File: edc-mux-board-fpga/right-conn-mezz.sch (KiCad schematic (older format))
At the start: 86 parts, among them J21 Device 10, J22 Device 13, J23 Device 11, J24 Device 14, J25 Left Mezzanine Board Connecto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, J26 Left Mezzanine Board Connecto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, J27 Device 12, J28 Device 15

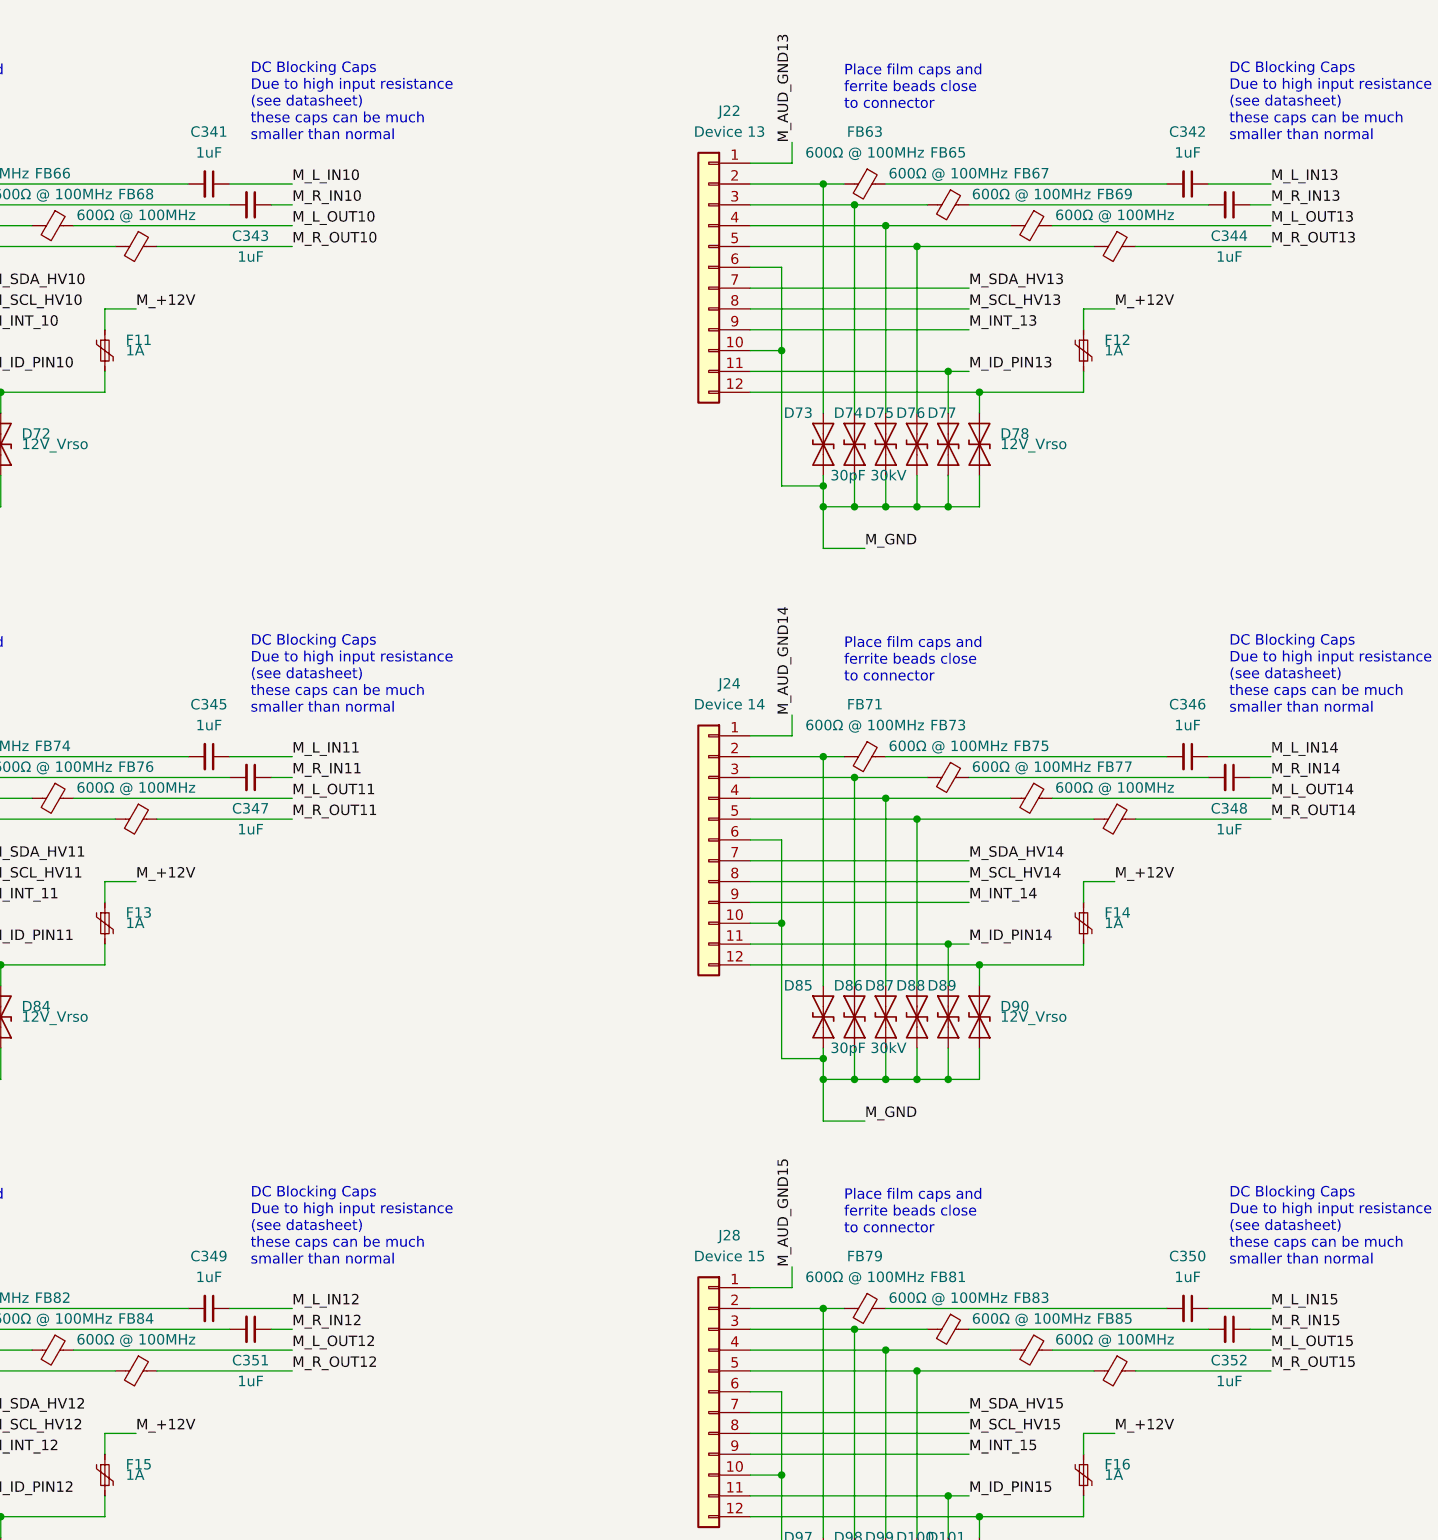
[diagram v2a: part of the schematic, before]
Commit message: assigned more footprints
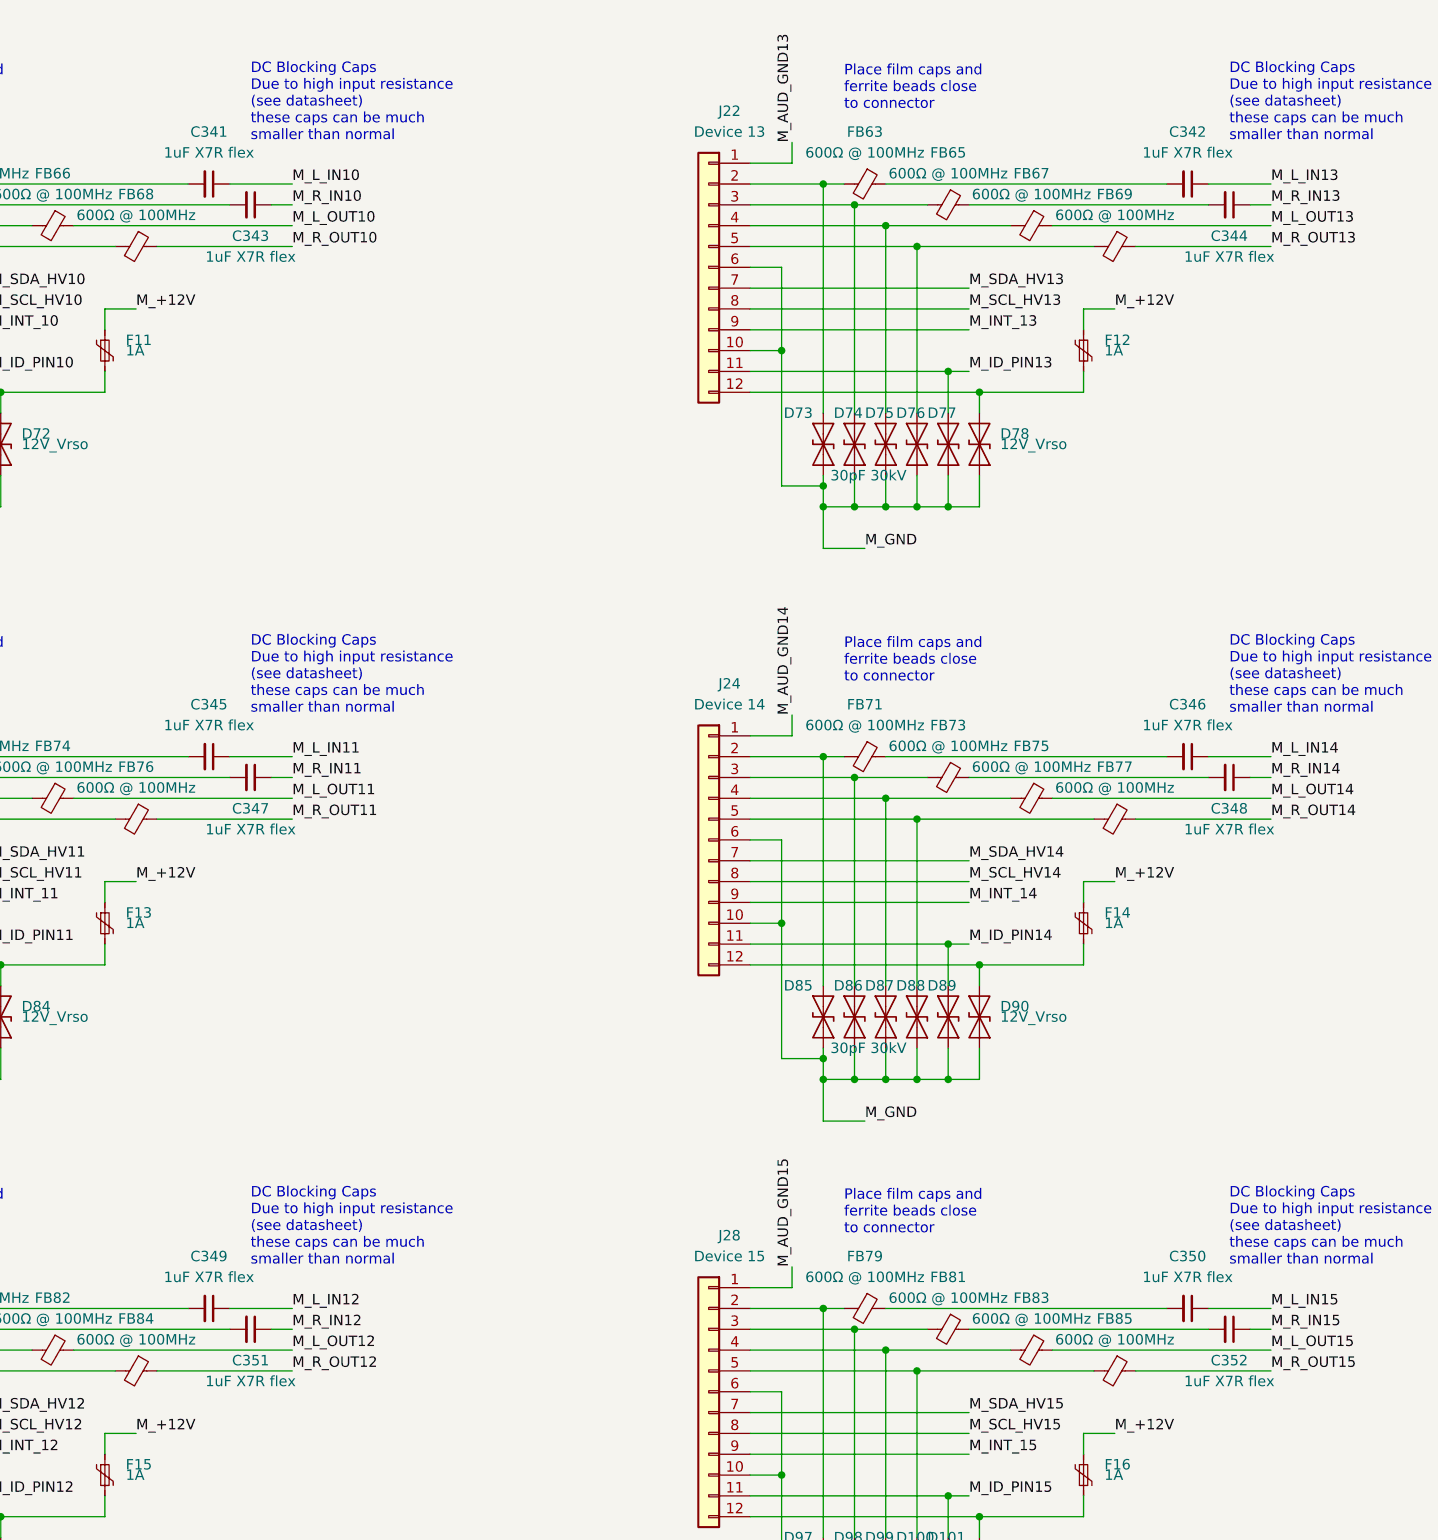
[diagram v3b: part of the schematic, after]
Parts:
- C341, C342, C343, C344, C345, C346, C347, C348, C349, C350, C351, C352: value 1uF -> 1uF X7R flex
- J21, J22, J23, J24, J27, J28: footprint Connector_PinHeader_1.27mm:PinHeader_2x06_P1.27mm_Vertical -> SW-TEConn:T4141012121-000; Manufacturer (none) -> TE Connectivity; Manufacturers Part Number (none) -> T4141012121-000
- J25: footprint (none) -> Connector_PinSocket_2.54mm:PinSocket_2x10_P2.54mm_Horizontal
- J26: footprint (none) -> Connector_PinHeader_2.54mm:PinHeader_2x10_P2.54mm_Vertical
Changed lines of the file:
@@
 F 0 "J21" H 700 2750 50  0000 C CNN
 F 1 "Device 10" H 700 2650 50  0000 C CNN
-F 2 "Connector_PinHeader_1.27mm:PinHeader_2x06_P1.27mm_Vertical" H 800 2000 50  0001 C CNN
-F 3 "~" H 800 2000 50  0001 C CNN
+F 2 "SW-TEConn:T4141012121-000" H 800 2000 50  0001 C CNN
+F 3 "https://www.te.com/commerce/DocumentDelivery/DDEController?Action=showdoc&DocId=Customer+Drawing%7FT4141012081000%7FA1%7Fpdf%7FEnglish%7FENG_CD_T4141012081000_A1.pdf%7FT4141012121-000" H 800 2000 50  0001 C CNN
+F 4 "TE Connectivity" H 0   0   50  0001 C CNN "Manufacturer"
+F 5 "T4141012121-000" H 0   0   50  0001 C CNN "Manufacturers Part Number"
 	1    800  2000
 	-1   0    0    -1
@@
 AR Path="/5CBF628A/61B47D43" Ref="C343"  Part="1"
 F 0 "C343" V 3450 1700 50  0000 C CNN
-F 1 "1uF" V 3550 1700 50  0000 C CNN
+F 1 "1uF X7R flex" V 3550 1700 50  0000 C CNN
 F 2 "Capacitor_SMD:C_0805_2012Metric" H 3300 1700 50  0001 C CNN
 F 3 "~" H 3300 1700 50  0001 C CNN
@@
 AR Path="/5CBF628A/61B47D54" Ref="C341"  Part="1"
 F 0 "C341" V 2850 1600 50  0000 C CNN
-F 1 "1uF" V 2950 1600 50  0000 C CNN
+F 1 "1uF X7R flex" V 2950 1600 50  0000 C CNN
 F 2 "Capacitor_SMD:C_0805_2012Metric" H 3100 1600 50  0001 C CNN
 F 3 "~" H 3100 1600 50  0001 C CNN
@@
 F 0 "J25" H 10450 7150 50  0000 C CNN
 F 1 "Left Mezzanine Board Connector (Daughterboard)" H 10450 3050 50  0000 C CNN
-F 2 "" H 10400 5150 50  0001 C CNN
+F 2 "Connector_PinSocket_2.54mm:PinSocket_2x10_P2.54mm_Horizontal" H 10400 5150 50  0001 C CNN
 F 3 "~" H 10400 5150 50  0001 C CNN
 	1    10400 5150
@@
 F 0 "J23" H 700 5500 50  0000 C CNN
 F 1 "Device 11" H 700 5400 50  0000 C CNN
-F 2 "Connector_PinHeader_1.27mm:PinHeader_2x06_P1.27mm_Vertical" H 800 4750 50  0001 C CNN
-F 3 "~" H 800 4750 50  0001 C CNN
+F 2 "SW-TEConn:T4141012121-000" H 800 4750 50  0001 C CNN
+F 3 "https://www.te.com/commerce/DocumentDelivery/DDEController?Action=showdoc&DocId=Customer+Drawing%7FT4141012081000%7FA1%7Fpdf%7FEnglish%7FENG_CD_T4141012081000_A1.pdf%7FT4141012121-000" H 800 4750 50  0001 C CNN
+F 4 "TE Connectivity" H 0   0   50  0001 C CNN "Manufacturer"
+F 5 "T4141012121-000" H 0   0   50  0001 C CNN "Manufacturers Part Number"
 	1    800  4750
 	-1   0    0    -1
@@
 AR Path="/5CBF628A/61B47E23" Ref="C347"  Part="1"
 F 0 "C347" V 3450 4450 50  0000 C CNN
-F 1 "1uF" V 3550 4450 50  0000 C CNN
+F 1 "1uF X7R flex" V 3550 4450 50  0000 C CNN
 F 2 "Capacitor_SMD:C_0805_2012Metric" H 3300 4450 50  0001 C CNN
 F 3 "~" H 3300 4450 50  0001 C CNN
@@
 AR Path="/5CBF628A/61B47E34" Ref="C345"  Part="1"
 F 0 "C345" V 2850 4350 50  0000 C CNN
-F 1 "1uF" V 2950 4350 50  0000 C CNN
+F 1 "1uF X7R flex" V 2950 4350 50  0000 C CNN
 F 2 "Capacitor_SMD:C_0805_2012Metric" H 3100 4350 50  0001 C CNN
 F 3 "~" H 3100 4350 50  0001 C CNN
@@
 F 0 "J27" H 700 8150 50  0000 C CNN
 F 1 "Device 12" H 700 8050 50  0000 C CNN
-F 2 "Connector_PinHeader_1.27mm:PinHeader_2x06_P1.27mm_Vertical" H 800 7400 50  0001 C CNN
-F 3 "~" H 800 7400 50  0001 C CNN
+F 2 "SW-TEConn:T4141012121-000" H 800 7400 50  0001 C CNN
+F 3 "https://www.te.com/commerce/DocumentDelivery/DDEController?Action=showdoc&DocId=Customer+Drawing%7FT4141012081000%7FA1%7Fpdf%7FEnglish%7FENG_CD_T4141012081000_A1.pdf%7FT4141012121-000" H 800 7400 50  0001 C CNN
+F 4 "TE Connectivity" H 0   0   50  0001 C CNN "Manufacturer"
+F 5 "T4141012121-000" H 0   0   50  0001 C CNN "Manufacturers Part Number"
 	1    800  7400
 	-1   0    0    -1
@@
 AR Path="/5CBF628A/61B47EF4" Ref="C351"  Part="1"
 F 0 "C351" V 3450 7100 50  0000 C CNN
-F 1 "1uF" V 3550 7100 50  0000 C CNN
+F 1 "1uF X7R flex" V 3550 7100 50  0000 C CNN
 F 2 "Capacitor_SMD:C_0805_2012Metric" H 3300 7100 50  0001 C CNN
 F 3 "~" H 3300 7100 50  0001 C CNN
@@
 AR Path="/5CBF628A/61B47F05" Ref="C349"  Part="1"
 F 0 "C349" V 2850 7000 50  0000 C CNN
-F 1 "1uF" V 2950 7000 50  0000 C CNN
+F 1 "1uF X7R flex" V 2950 7000 50  0000 C CNN
 F 2 "Capacitor_SMD:C_0805_2012Metric" H 3100 7000 50  0001 C CNN
 F 3 "~" H 3100 7000 50  0001 C CNN
@@
 F 0 "J22" H 5400 2750 50  0000 C CNN
 F 1 "Device 13" H 5400 2650 50  0000 C CNN
-F 2 "Connector_PinHeader_1.27mm:PinHeader_2x06_P1.27mm_Vertical" H 5500 2000 50  0001 C CNN
-F 3 "~" H 5500 2000 50  0001 C CNN
+F 2 "SW-TEConn:T4141012121-000" H 5500 2000 50  0001 C CNN
+F 3 "https://www.te.com/commerce/DocumentDelivery/DDEController?Action=showdoc&DocId=Customer+Drawing%7FT4141012081000%7FA1%7Fpdf%7FEnglish%7FENG_CD_T4141012081000_A1.pdf%7FT4141012121-000" H 5500 2000 50  0001 C CNN
+F 4 "TE Connectivity" H 0   0   50  0001 C CNN "Manufacturer"
+F 5 "T4141012121-000" H 0   0   50  0001 C CNN "Manufacturers Part Number"
 	1    5500 2000
 	-1   0    0    -1
@@
 AR Path="/5CBF628A/61B47FC5" Ref="C344"  Part="1"
 F 0 "C344" V 8150 1700 50  0000 C CNN
-F 1 "1uF" V 8250 1700 50  0000 C CNN
+F 1 "1uF X7R flex" V 8250 1700 50  0000 C CNN
 F 2 "Capacitor_SMD:C_0805_2012Metric" H 8000 1700 50  0001 C CNN
 F 3 "~" H 8000 1700 50  0001 C CNN
@@
 AR Path="/5CBF628A/61B47FD6" Ref="C342"  Part="1"
 F 0 "C342" V 7550 1600 50  0000 C CNN
-F 1 "1uF" V 7650 1600 50  0000 C CNN
+F 1 "1uF X7R flex" V 7650 1600 50  0000 C CNN
 F 2 "Capacitor_SMD:C_0805_2012Metric" H 7800 1600 50  0001 C CNN
 F 3 "~" H 7800 1600 50  0001 C CNN
@@
 F 0 "J24" H 5400 5500 50  0000 C CNN
 F 1 "Device 14" H 5400 5400 50  0000 C CNN
-F 2 "Connector_PinHeader_1.27mm:PinHeader_2x06_P1.27mm_Vertical" H 5500 4750 50  0001 C CNN
-F 3 "~" H 5500 4750 50  0001 C CNN
+F 2 "SW-TEConn:T4141012121-000" H 5500 4750 50  0001 C CNN
+F 3 "https://www.te.com/commerce/DocumentDelivery/DDEController?Action=showdoc&DocId=Customer+Drawing%7FT4141012081000%7FA1%7Fpdf%7FEnglish%7FENG_CD_T4141012081000_A1.pdf%7FT4141012121-000" H 5500 4750 50  0001 C CNN
+F 4 "TE Connectivity" H 0   0   50  0001 C CNN "Manufacturer"
+F 5 "T4141012121-000" H 0   0   50  0001 C CNN "Manufacturers Part Number"
 	1    5500 4750
 	-1   0    0    -1
@@
 AR Path="/5CBF628A/61B48096" Ref="C348"  Part="1"
 F 0 "C348" V 8150 4450 50  0000 C CNN
-F 1 "1uF" V 8250 4450 50  0000 C CNN
+F 1 "1uF X7R flex" V 8250 4450 50  0000 C CNN
 F 2 "Capacitor_SMD:C_0805_2012Metric" H 8000 4450 50  0001 C CNN
 F 3 "~" H 8000 4450 50  0001 C CNN
@@
 AR Path="/5CBF628A/61B480A7" Ref="C346"  Part="1"
 F 0 "C346" V 7550 4350 50  0000 C CNN
-F 1 "1uF" V 7650 4350 50  0000 C CNN
+F 1 "1uF X7R flex" V 7650 4350 50  0000 C CNN
 F 2 "Capacitor_SMD:C_0805_2012Metric" H 7800 4350 50  0001 C CNN
 F 3 "~" H 7800 4350 50  0001 C CNN
@@
 F 0 "J28" H 5400 8150 50  0000 C CNN
 F 1 "Device 15" H 5400 8050 50  0000 C CNN
-F 2 "Connector_PinHeader_1.27mm:PinHeader_2x06_P1.27mm_Vertical" H 5500 7400 50  0001 C CNN
-F 3 "~" H 5500 7400 50  0001 C CNN
+F 2 "SW-TEConn:T4141012121-000" H 5500 7400 50  0001 C CNN
+F 3 "https://www.te.com/commerce/DocumentDelivery/DDEController?Action=showdoc&DocId=Customer+Drawing%7FT4141012081000%7FA1%7Fpdf%7FEnglish%7FENG_CD_T4141012081000_A1.pdf%7FT4141012121-000" H 5500 7400 50  0001 C CNN
+F 4 "TE Connectivity" H 0   0   50  0001 C CNN "Manufacturer"
+F 5 "T4141012121-000" H 0   0   50  0001 C CNN "Manufacturers Part Number"
 	1    5500 7400
 	-1   0    0    -1
@@
 AR Path="/5CBF628A/61B48167" Ref="C352"  Part="1"
 F 0 "C352" V 8150 7100 50  0000 C CNN
-F 1 "1uF" V 8250 7100 50  0000 C CNN
+F 1 "1uF X7R flex" V 8250 7100 50  0000 C CNN
 F 2 "Capacitor_SMD:C_0805_2012Metric" H 8000 7100 50  0001 C CNN
 F 3 "~" H 8000 7100 50  0001 C CNN
@@
 AR Path="/5CBF628A/61B48178" Ref="C350"  Part="1"
 F 0 "C350" V 7550 7000 50  0000 C CNN
-F 1 "1uF" V 7650 7000 50  0000 C CNN
+F 1 "1uF X7R flex" V 7650 7000 50  0000 C CNN
 F 2 "Capacitor_SMD:C_0805_2012Metric" H 7800 7000 50  0001 C CNN
 F 3 "~" H 7800 7000 50  0001 C CNN
@@
 F 0 "J26" H 14000 7150 50  0000 C CNN
 F 1 "Left Mezzanine Board Connector (Motherboard)" H 14000 3050 50  0000 C CNN
-F 2 "" H 13950 5150 50  0001 C CNN
+F 2 "Connector_PinHeader_2.54mm:PinHeader_2x10_P2.54mm_Vertical" H 13950 5150 50  0001 C CNN
 F 3 "~" H 13950 5150 50  0001 C CNN
 	1    13950 5150
